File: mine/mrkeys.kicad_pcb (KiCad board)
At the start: 2 copper layers, 179.3 x 121.4 mm, 82 parts

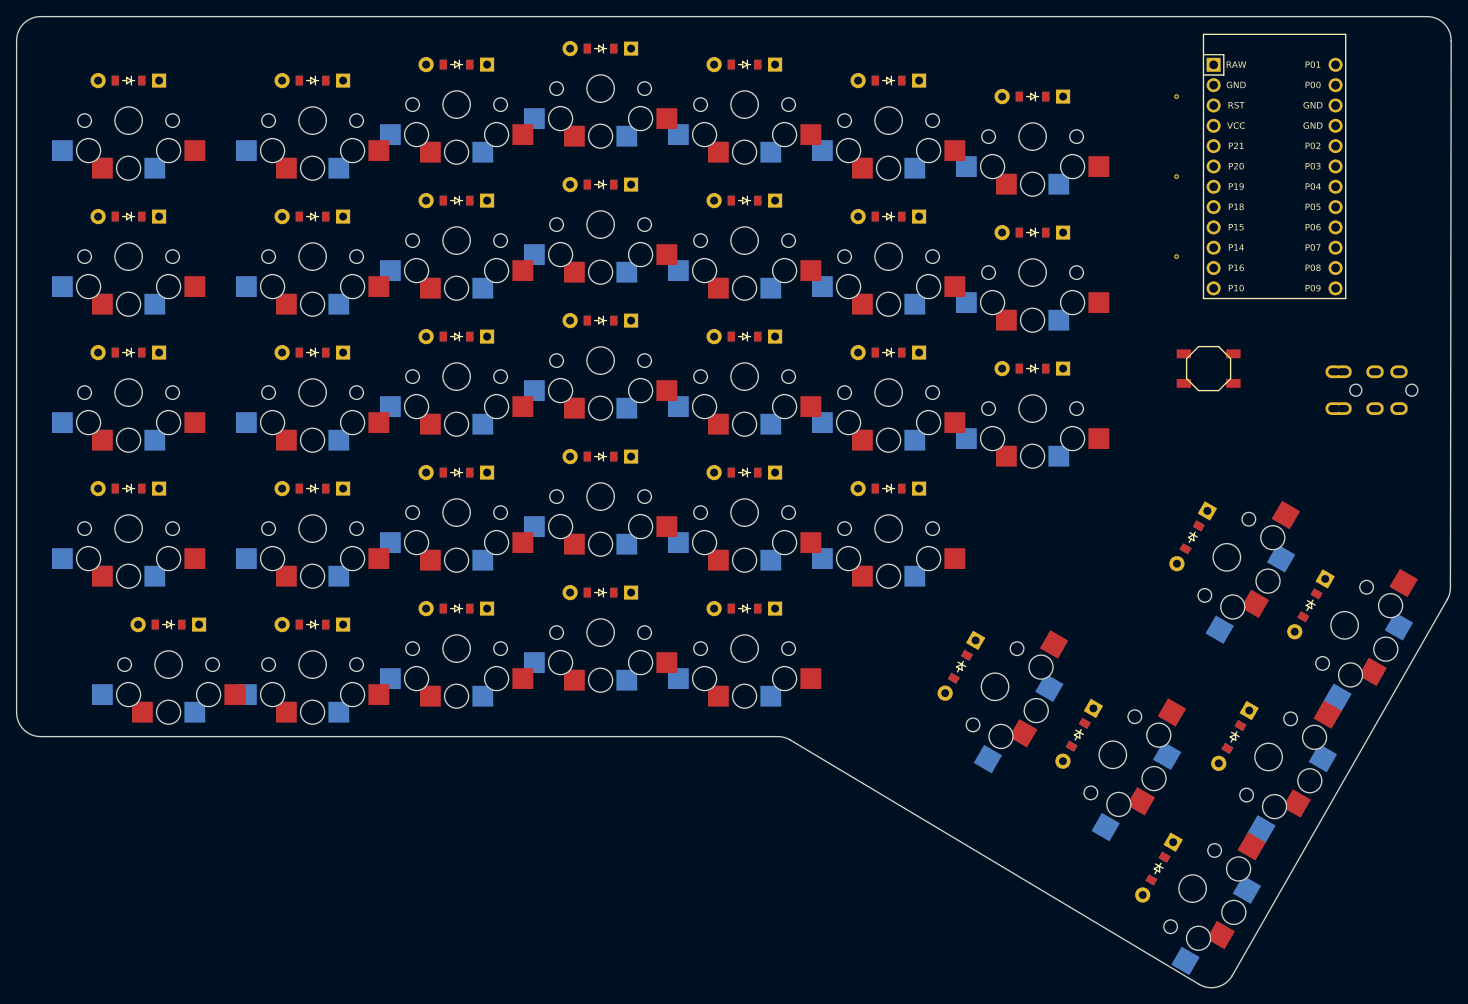
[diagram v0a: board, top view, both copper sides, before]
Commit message: Added RGB and moved diode. Also moved VIAs.
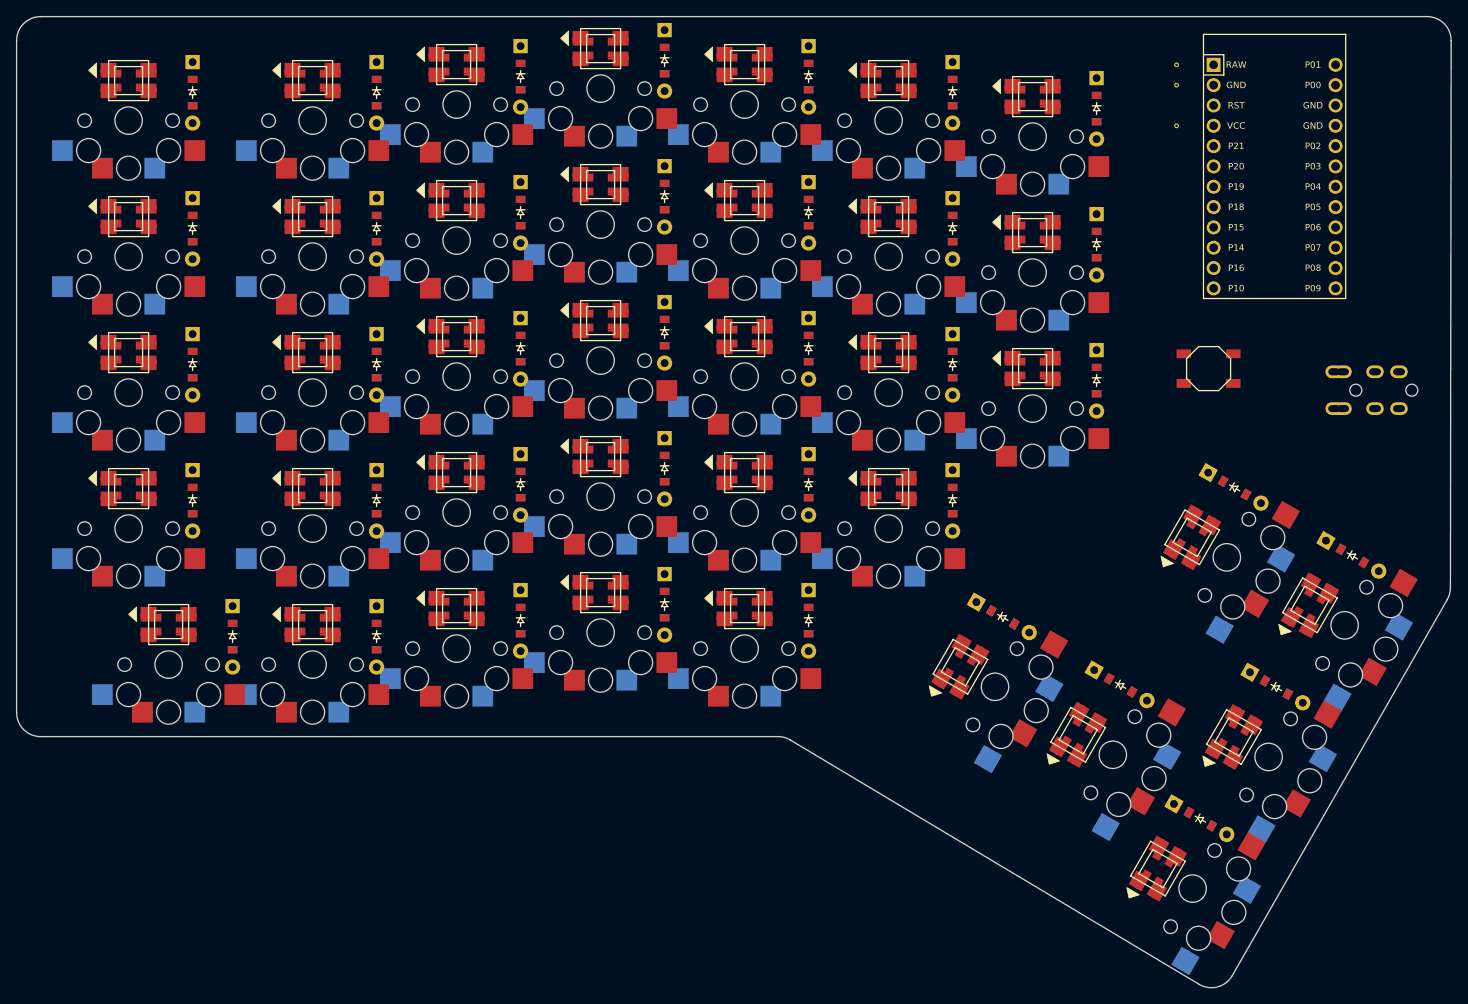
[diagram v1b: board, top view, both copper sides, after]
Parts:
- removed the REF** at (144.0, -51.0)
- removed the REF** at (144.0, -61.0)
- removed the REF** at (144.0, -71.0)
- added LED1: , WS2812B, F.Cu at (18.0, -5.00)
- added LED10: , WS2812B, F.Cu at (36.0, -73.0)
- added LED11: , WS2812B, F.Cu at (54.0, -7.00)
- added LED12: , WS2812B, F.Cu at (54.0, -24.0)
- added LED13: , WS2812B, F.Cu at (54.0, -41.0)
- added LED14: , WS2812B, F.Cu at (54.0, -58.0)
- added LED15: , WS2812B, F.Cu at (54.0, -75.0)
- added LED16: , WS2812B, F.Cu at (72.0, -9.00)
- added LED17: , WS2812B, F.Cu at (72.0, -26.0)
- added LED18: , WS2812B, F.Cu at (72.0, -43.0)
- added LED19: , WS2812B, F.Cu at (72.0, -60.0)
- added LED2: , WS2812B, F.Cu at (13.0, -22.0)
- added LED20: , WS2812B, F.Cu at (72.0, -77.0)
- added LED21: , WS2812B, F.Cu at (90.0, -7.00)
- added LED22: , WS2812B, F.Cu at (90.0, -24.0)
- added LED23: , WS2812B, F.Cu at (90.0, -41.0)
- added LED24: , WS2812B, F.Cu at (90.0, -58.0)
- added LED25: , WS2812B, F.Cu at (90.0, -75.0)
- added LED26: , WS2812B, F.Cu at (108.0, -22.0)
- added LED27: , WS2812B, F.Cu at (108.0, -39.0)
- added LED28: , WS2812B, F.Cu at (108.0, -56.0)
- added LED29: , WS2812B, F.Cu at (108.0, -73.0)
- added LED3: , WS2812B, F.Cu at (13.0, -39.0)
- added LED30: , WS2812B, F.Cu at (126.0, -37.0)
- added LED31: , WS2812B, F.Cu at (126.0, -54.0)
- added LED32: , WS2812B, F.Cu at (126.0, -71.0)
- added LED33: , WS2812B, F.Cu at (141.7, 25.5)
- added LED34: , WS2812B, F.Cu at (131.7, 8.77)
- added LED35: , WS2812B, F.Cu at (117.0, 0.27)
- added LED36: , WS2812B, F.Cu at (151.2, 9.05)
- added LED37: , WS2812B, F.Cu at (160.7, -7.41)
- added LED38: , WS2812B, F.Cu at (145.9, -15.9)
- added LED4: , WS2812B, F.Cu at (13.0, -56.0)
- added LED5: , WS2812B, F.Cu at (13.0, -73.0)
- added LED6: , WS2812B, F.Cu at (36.0, -5.00)
- added LED7: , WS2812B, F.Cu at (36.0, -22.0)
- added LED8: , WS2812B, F.Cu at (36.0, -39.0)
- added LED9: , WS2812B, F.Cu at (36.0, -56.0)
- added REF**: VIA-0.6mm, VIA-0.6mm, F.Cu at (144.0, -75.0)
- added REF**: VIA-0.6mm, VIA-0.6mm, F.Cu at (144.0, -67.3)
- added REF**: VIA-0.6mm, VIA-0.6mm, F.Cu at (144.0, -72.4)
- moved D1 8.14 mm to (26.0, -3.50), turned to 270 degrees
- moved D10 8.14 mm to (44.0, -71.5), turned to 270 degrees
- moved D11 8.14 mm to (62.0, -5.50), turned to 270 degrees
- moved D12 8.14 mm to (62.0, -22.5), turned to 270 degrees
- moved D13 8.14 mm to (62.0, -39.5), turned to 270 degrees
- moved D14 8.14 mm to (62.0, -56.5), turned to 270 degrees
- moved D15 8.14 mm to (62.0, -73.5), turned to 270 degrees
- moved D16 8.14 mm to (80.0, -7.50), turned to 270 degrees
- moved D17 8.14 mm to (80.0, -24.5), turned to 270 degrees
- moved D18 8.14 mm to (80.0, -41.5), turned to 270 degrees
- moved D19 8.14 mm to (80.0, -58.5), turned to 270 degrees
- moved D2 8.14 mm to (21.0, -20.5), turned to 270 degrees
- moved D20 8.14 mm to (80.0, -75.5), turned to 270 degrees
- moved D21 8.14 mm to (98.0, -5.50), turned to 270 degrees
- moved D22 8.14 mm to (98.0, -22.5), turned to 270 degrees
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
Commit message: Fixed orientation of thumbcluster keys.
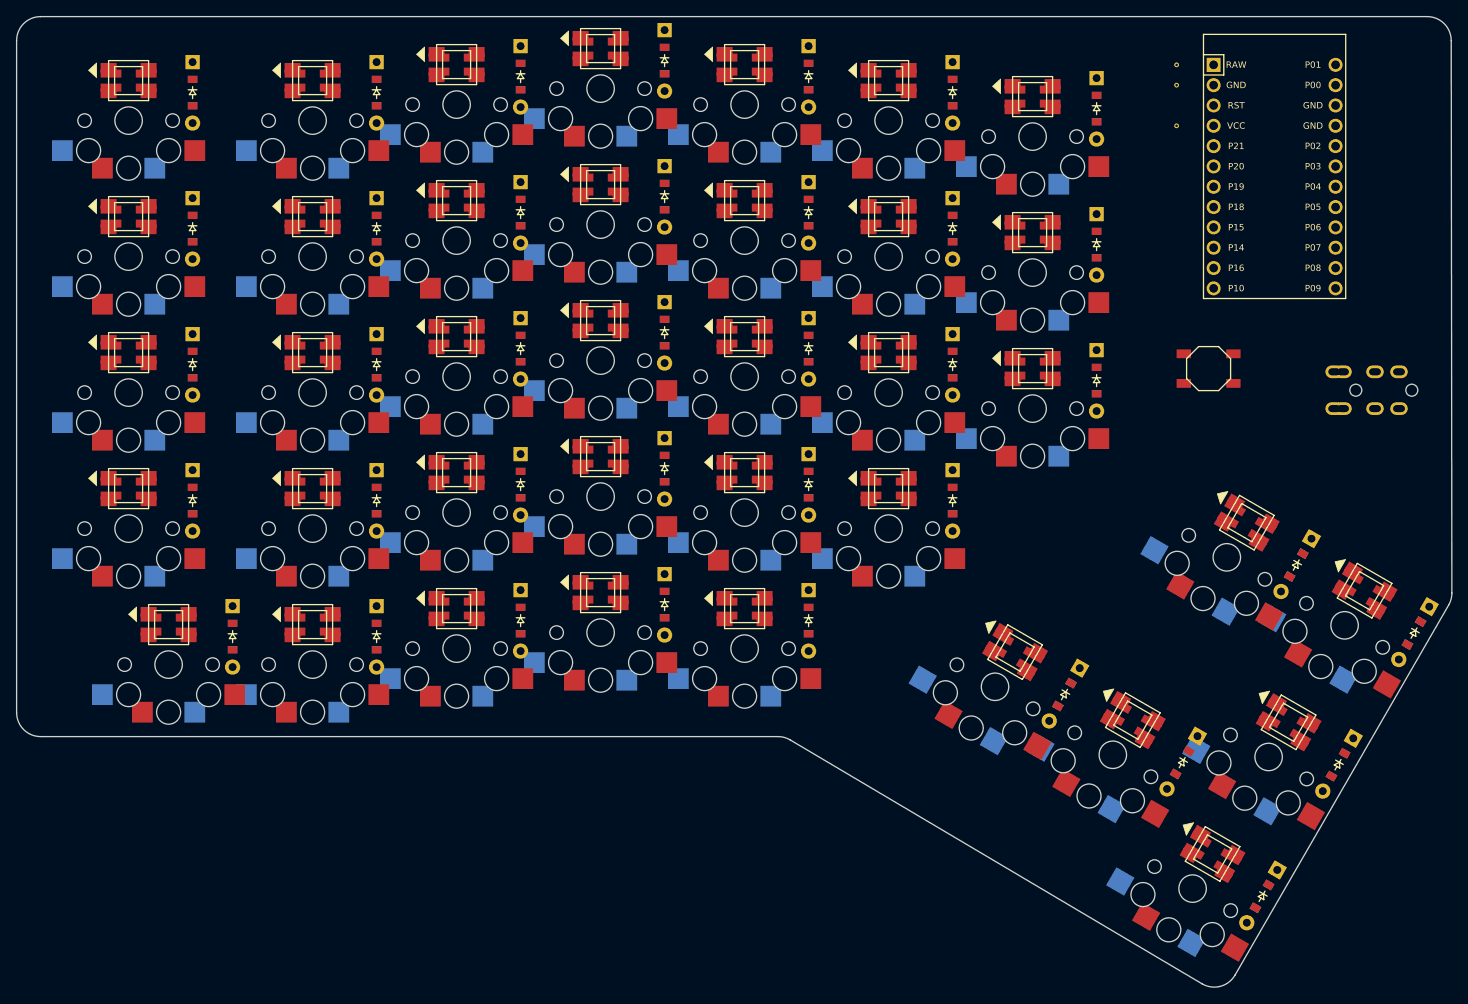
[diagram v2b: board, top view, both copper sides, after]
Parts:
- moved D34 12.3 mm to (144.7, 12.2), turned to 600 degrees
- moved D35 12.3 mm to (130.0, 3.74), turned to 600 degrees
- moved D36 12.3 mm to (164.2, 12.5), turned to 600 degrees
- moved D37 12.3 mm to (173.7, -3.94), turned to 600 degrees
- moved D33 12.3 mm to (154.7, 29.0), turned to 600 degrees
- moved D38 12.3 mm to (159.0, -12.4), turned to 600 degrees
- moved LED33 7.07 mm to (148.5, 23.7), turned to 510 degrees
- moved LED34 7.07 mm to (138.5, 6.94), turned to 510 degrees
- moved LED35 7.07 mm to (123.8, -1.56), turned to 510 degrees
- moved LED36 7.07 mm to (158.0, 7.22), turned to 510 degrees
- moved LED37 7.07 mm to (167.5, -9.24), turned to 510 degrees
- moved LED38 7.07 mm to (152.8, -17.7), turned to 510 degrees
- turned S33 to 510 degrees
- turned S34 to 510 degrees
- turned S35 to 510 degrees
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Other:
- board size 179.3 x 121.4 mm -> 179.4 x 121.3 mm
